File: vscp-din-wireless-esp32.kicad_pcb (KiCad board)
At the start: 2 copper layers, 64.8 x 51 mm, 18 parts, among them J1 Conn_Left_I2C, J2 Conn_Right_Power, J3 Conn_01x06, U1 ESP32-WROOM-32D

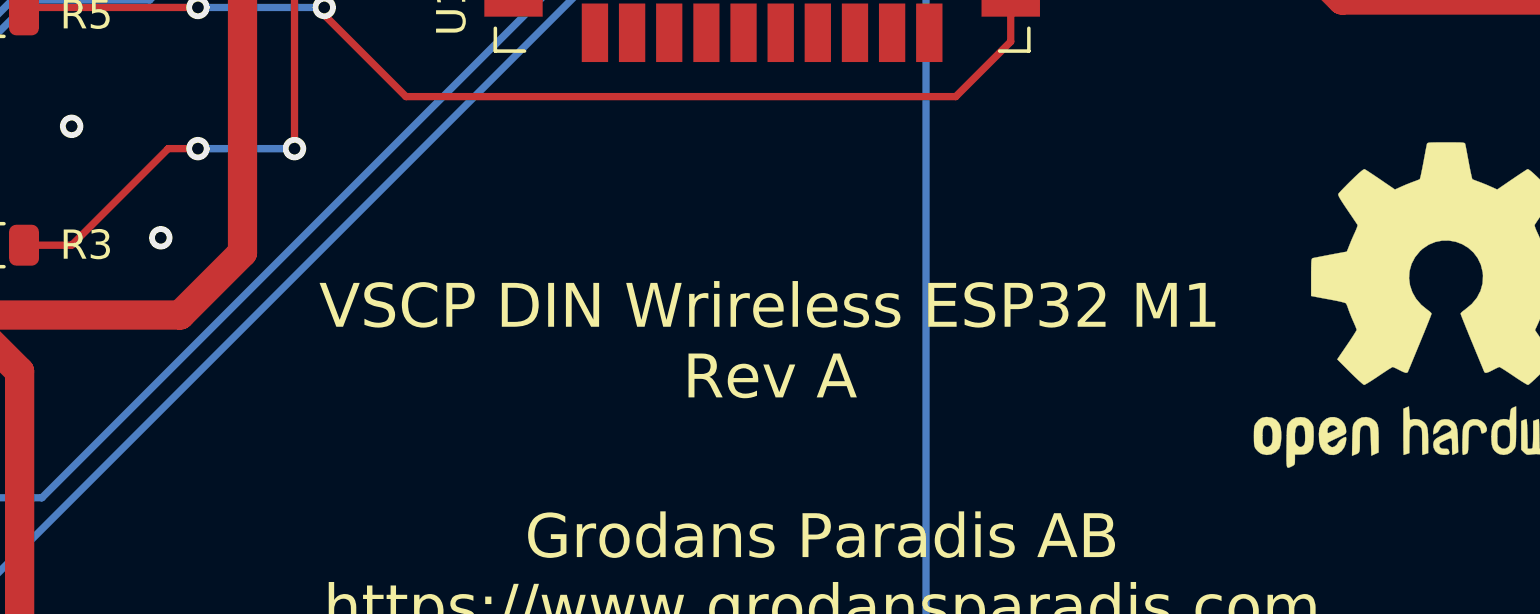
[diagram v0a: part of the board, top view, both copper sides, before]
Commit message: Fixed module name
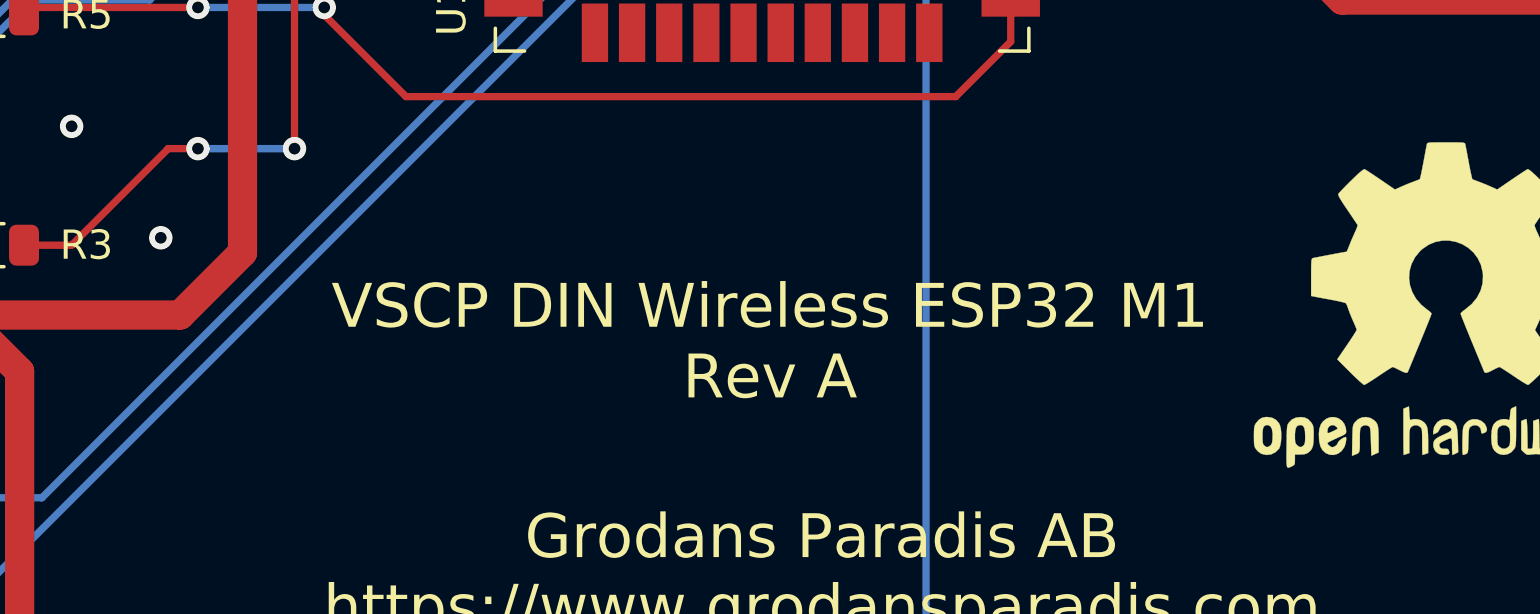
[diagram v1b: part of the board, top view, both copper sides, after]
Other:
- board text added: "VSCP DIN Wireless ESP32 M1 Rev A"
- board text removed: "VSCP DIN Wrireless ESP32 M1 Rev A"
